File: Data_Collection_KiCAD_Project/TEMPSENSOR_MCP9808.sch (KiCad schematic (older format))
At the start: 2 parts

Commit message: Fixed Component Libraries
Changed over from project specific to global libraries.
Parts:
- C?: symbol Data_Collection_KiCAD_Project-rescue:C-Device -> Data_Collection_KiCAD_Project-rescue:C-Device-Data_Collection_KiCAD_Project-rescue
- U?: symbol Data_Collection_KiCAD_Project-rescue:MCP9808_MSOP-Sensor_Temperature -> Data_Collection_KiCAD_Project-rescue:MCP9808_MSOP-Sensor_Temperature-Data_Collection_KiCAD_Project-rescue
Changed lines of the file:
@@
 $Descr A4 11693 8268
 encoding utf-8
-Sheet 3 10
+Sheet 3 9
 Title "MCP9608 Temperature Sensor"
 Date "2021-10-01"
@@
 $EndDescr
 $Comp
-L Data_Collection_KiCAD_Project-rescue:GND-power #PWR?
+L Data_Collection_KiCAD_Project-rescue:GND-power-Data_Collection_KiCAD_Project-rescue #PWR?
 U 1 1 6160E311
 P 5500 4150
@@
 $EndComp
 $Comp
-L Data_Collection_KiCAD_Project-rescue:+3.3V-power #PWR?
+L Data_Collection_KiCAD_Project-rescue:+3.3V-power-Data_Collection_KiCAD_Project-rescue #PWR?
 U 1 1 6160E323
 P 5950 2950
@@
 Temp Sensor
 $Comp
-L Data_Collection_KiCAD_Project-rescue:C-Device C?
+L Data_Collection_KiCAD_Project-rescue:C-Device-Data_Collection_KiCAD_Project-rescue C?
 U 1 1 6160E331
 P 6500 3600
@@
 	5500 4050 5500 4150
 $Comp
-L Data_Collection_KiCAD_Project-rescue:MCP9808_MSOP-Sensor_Temperature U?
+L Data_Collection_KiCAD_Project-rescue:MCP9808_MSOP-Sensor_Temperature-Data_Collection_KiCAD_Project-rescue U?
 U 1 1 6160E30B
 P 5500 3550
@@
 Connection ~ 5950 3000
 $Comp
-L Data_Collection_KiCAD_Project-rescue:GND-power #PWR?
+L Data_Collection_KiCAD_Project-rescue:GND-power-Data_Collection_KiCAD_Project-rescue #PWR?
 U 1 1 618848DE
 P 6500 3750

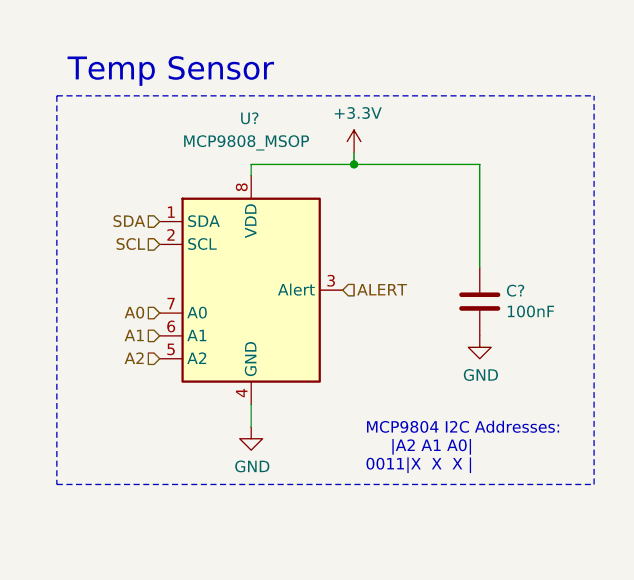
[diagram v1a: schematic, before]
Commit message: footprint and value changes
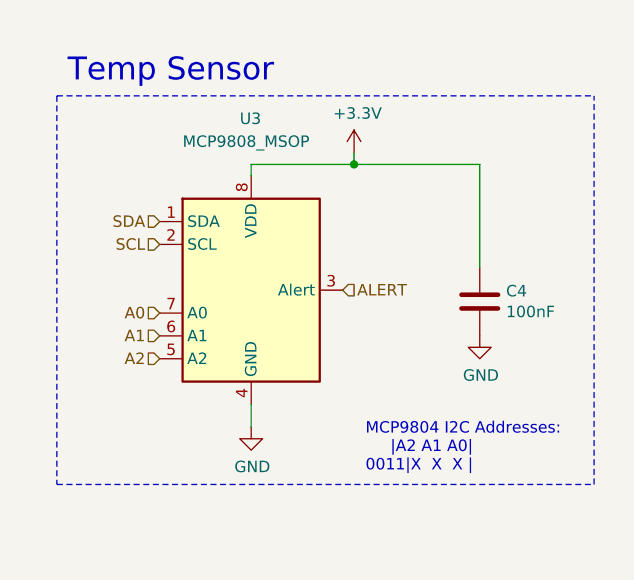
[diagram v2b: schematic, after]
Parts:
- C4: renamed from C?; footprint (none) -> Capacitor_SMD:C_0603_1608Metric
- gave numbers to parts that had none: 1
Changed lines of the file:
@@
 P 5500 4150
 AR Path="/6160E311" Ref="#PWR?"  Part="1"
-AR Path="/615C1FB4/6160E311" Ref="#PWR?"  Part="1"
-F 0 "#PWR?" H 5500 3900 50  0001 C CNN
+AR Path="/615C1FB4/6160E311" Ref="#PWR020"  Part="1"
+F 0 "#PWR020" H 5500 3900 50  0001 C CNN
 F 1 "GND" H 5505 3977 50  0000 C CNN
 F 2 "" H 5500 4150 50  0001 C CNN
@@
 P 5950 2950
 AR Path="/6160E323" Ref="#PWR?"  Part="1"
-AR Path="/615C1FB4/6160E323" Ref="#PWR?"  Part="1"
-F 0 "#PWR?" H 5950 2800 50  0001 C CNN
+AR Path="/615C1FB4/6160E323" Ref="#PWR021"  Part="1"
+F 0 "#PWR021" H 5950 2800 50  0001 C CNN
 F 1 "+3.3V" H 5965 3123 50  0000 C CNN
 F 2 "" H 5950 2950 50  0001 C CNN
@@
 P 6500 3600
 AR Path="/6160E331" Ref="C?"  Part="1"
-AR Path="/615C1FB4/6160E331" Ref="C?"  Part="1"
-F 0 "C?" H 6615 3646 50  0000 L CNN
+AR Path="/615C1FB4/6160E331" Ref="C4"  Part="1"
+F 0 "C4" H 6615 3646 50  0000 L CNN
 F 1 "100nF" H 6615 3555 50  0000 L CNN
-F 2 "" H 6538 3450 50  0001 C CNN
+F 2 "Capacitor_SMD:C_0603_1608Metric" H 6538 3450 50  0001 C CNN
 F 3 "~" H 6500 3600 50  0001 C CNN
 	1    6500 3600
@@
 P 5500 3550
 AR Path="/6160E30B" Ref="U?"  Part="1"
-AR Path="/615C1FB4/6160E30B" Ref="U?"  Part="1"
-F 0 "U?" H 5450 4300 50  0000 L CNN
+AR Path="/615C1FB4/6160E30B" Ref="U3"  Part="1"
+F 0 "U3" H 5450 4300 50  0000 L CNN
 F 1 "MCP9808_MSOP" H 5200 4200 50  0000 L CNN
 F 2 "Package_SO:MSOP-8_3x3mm_P0.65mm" H 5500 3550 50  0001 C CNN
@@
 P 6500 3750
 AR Path="/618848DE" Ref="#PWR?"  Part="1"
-AR Path="/615C1FB4/618848DE" Ref="#PWR?"  Part="1"
-F 0 "#PWR?" H 6500 3500 50  0001 C CNN
+AR Path="/615C1FB4/618848DE" Ref="#PWR022"  Part="1"
+F 0 "#PWR022" H 6500 3500 50  0001 C CNN
 F 1 "GND" H 6505 3577 50  0000 C CNN
 F 2 "" H 6500 3750 50  0001 C CNN

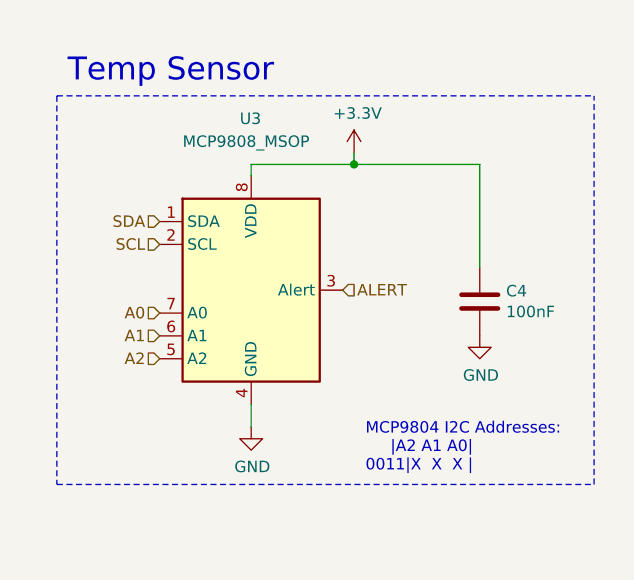
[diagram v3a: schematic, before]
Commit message: footprint changes
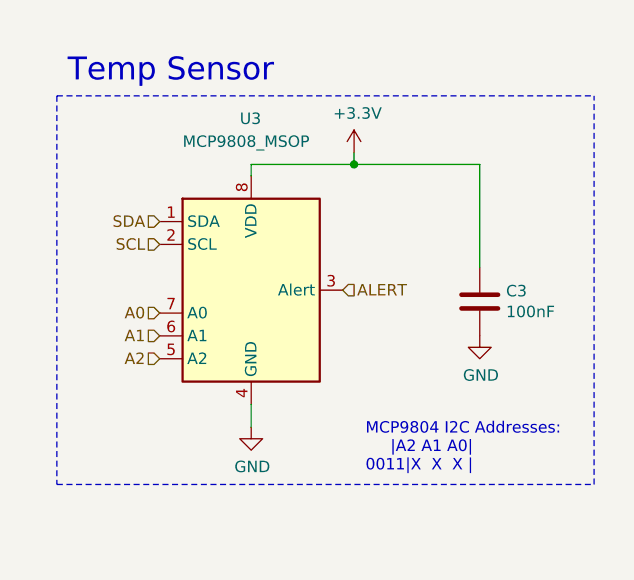
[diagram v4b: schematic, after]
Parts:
- renumbered C4 to C3
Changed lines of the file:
@@
 P 5500 4150
 AR Path="/6160E311" Ref="#PWR?"  Part="1"
-AR Path="/615C1FB4/6160E311" Ref="#PWR020"  Part="1"
-F 0 "#PWR020" H 5500 3900 50  0001 C CNN
+AR Path="/615C1FB4/6160E311" Ref="#PWR013"  Part="1"
+F 0 "#PWR013" H 5500 3900 50  0001 C CNN
 F 1 "GND" H 5505 3977 50  0000 C CNN
 F 2 "" H 5500 4150 50  0001 C CNN
@@
 P 5950 2950
 AR Path="/6160E323" Ref="#PWR?"  Part="1"
-AR Path="/615C1FB4/6160E323" Ref="#PWR021"  Part="1"
-F 0 "#PWR021" H 5950 2800 50  0001 C CNN
+AR Path="/615C1FB4/6160E323" Ref="#PWR014"  Part="1"
+F 0 "#PWR014" H 5950 2800 50  0001 C CNN
 F 1 "+3.3V" H 5965 3123 50  0000 C CNN
 F 2 "" H 5950 2950 50  0001 C CNN
@@
 P 6500 3600
 AR Path="/6160E331" Ref="C?"  Part="1"
-AR Path="/615C1FB4/6160E331" Ref="C4"  Part="1"
-F 0 "C4" H 6615 3646 50  0000 L CNN
+AR Path="/615C1FB4/6160E331" Ref="C3"  Part="1"
+F 0 "C3" H 6615 3646 50  0000 L CNN
 F 1 "100nF" H 6615 3555 50  0000 L CNN
 F 2 "Capacitor_SMD:C_0603_1608Metric" H 6538 3450 50  0001 C CNN
@@
 P 6500 3750
 AR Path="/618848DE" Ref="#PWR?"  Part="1"
-AR Path="/615C1FB4/618848DE" Ref="#PWR022"  Part="1"
-F 0 "#PWR022" H 6500 3500 50  0001 C CNN
+AR Path="/615C1FB4/618848DE" Ref="#PWR015"  Part="1"
+F 0 "#PWR015" H 6500 3500 50  0001 C CNN
 F 1 "GND" H 6505 3577 50  0000 C CNN
 F 2 "" H 6500 3750 50  0001 C CNN
